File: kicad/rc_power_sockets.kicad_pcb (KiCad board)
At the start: 2 copper layers, 17 parts, among them IC1 ATTINY85-P, J1 Motion Sensor, J2 Radio 433MHZ, P1 ICSP, Q1 N-Channel Mosfet, Q2 P-Channel Mosfet, SW1 SPST, U1 LDO 3v3 Voltage Regulator

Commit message: GND pin on header
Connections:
- J2 pad 1: Net-(C1-Pad1) -> GND
- J2 pad 3: GND -> Net-(C1-Pad1)
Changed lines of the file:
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@@
     (pad_to_mask_clearance 0.2)
     (aux_axis_origin 0 0)
-    (visible_elements FFFFF77F)
+    (visible_elements 7FFFFFFF)
     (pcbplotparams
       (layerselection 0x00030_80000001)
@@
     (fp_line (start -1.55 -1.55) (end 1.55 -1.55) (layer F.SilkS) (width 0.15))
     (pad 1 thru_hole rect (at 0 0) (size 2.032 1.7272) (drill 1.016) (layers *.Cu *.Mask F.SilkS)
-      (net 1 "Net-(C1-Pad1)"))
+      (net 2 GND))
     (pad 2 thru_hole oval (at 0 2.54) (size 2.032 1.7272) (drill 1.016) (layers *.Cu *.Mask F.SilkS)
       (net 9 /RADIO_DATA))
     (pad 3 thru_hole oval (at 0 5.08) (size 2.032 1.7272) (drill 1.016) (layers *.Cu *.Mask F.SilkS)
-      (net 2 GND))
+      (net 1 "Net-(C1-Pad1)"))
     (model Pin_Headers.3dshapes/Pin_Header_Straight_1x03.wrl
       (at (xyz 0 -0.1 0))

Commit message: SMD ATTiny
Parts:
- added C3: 0.1uf, Capacitors_SMD:C_1206_HandSoldering, F.Cu at (146.1, 82.5)
- IC1: value ATTINY85-P -> ATTINY85-S; footprint Housings_DIP:DIP-8_W7.62mm_LongPads -> SMD_Packages:SOIC-8-N
- J1, J2: footprint Pin_Headers:Pin_Header_Straight_1x03 -> Socket_Strips:Socket_Strip_Straight_1x03
- SW1: value SPST -> Power Switch; footprint Wire_Pads:SolderWirePad_2x_2-5mmDrill -> Buttons_Switches_ThroughHole:SW_Micro_SPST_Angled
- moved SW1 56.6 mm to (118.1, 106.7), turned to 0 degrees
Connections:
- SW1 pad 1: Net-(J1-Pad3) -> +BATT

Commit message: Use existing parts
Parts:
- added R5: 100K, Resistors_SMD:R_0805_HandSoldering, F.Cu at (86.4, 96.5)
- added RV1: POT, Potentiometers:Potentiometer_WirePads_largePads, F.Cu at (92.7, 100.3)
- C1, C2, C3: footprint Capacitors_SMD:C_1206_HandSoldering -> Capacitors_SMD:C_0805_HandSoldering
- D1, D2: footprint SMD_Packages:SMD-1206_Pol -> Diodes_SMD:SOD-123
- Q1: value N-Channel Mosfet -> Q_NMOS_GSD
- Q2: value P-Channel Mosfet -> Q_PMOS_GSD
- R1, R2, R3, R4: footprint Resistors_SMD:R_1206_HandSoldering -> Resistors_SMD:R_0805_HandSoldering
- SW1: footprint Buttons_Switches_ThroughHole:SW_Micro_SPST_Angled -> Buttons_Switches_ThroughHole:SW_Micro_SPST
- U1: value LDO 3v3 Voltage Regulator -> MCP1700T-3302E/TT
- moved D1 4.02 mm to (156.2, 91.4)
- moved D2 1.80 mm to (156.2, 99.1)
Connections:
- net +BATT renamed VCC
- IC1 pad 2: Net-(IC1-Pad2) -> /ADC3
- Q1 pad 2: Net-(Q1-Pad2) -> GND
- Q1 pad 3: GND -> Net-(Q1-Pad3)
- Q2 pad 1: Net-(Q1-Pad2) -> Net-(Q1-Pad3)
- R2 pad 2: Net-(Q1-Pad2) -> Net-(Q1-Pad3)

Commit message: 50mm x 50mm
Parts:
- moved R5 142.0 mm to (226.0, 71.0)
- moved RV1 134.7 mm to (225.0, 75.0)
- moved SW1 99.2 mm to (217.0, 99.0)
- moved J2 95.8 mm to (215.0, 71.0)
- moved Q1 71.8 mm to (206.0, 79.0)
- moved R3 71.0 mm to (200.0, 80.0), turned to 180 degrees
- moved Q2 70.5 mm to (211.0, 79.0)
- moved R1 66.8 mm to (200.0, 75.0), turned to 180 degrees
- moved IC1 66.5 mm to (206.0, 88.0)
- moved R4 65.7 mm to (199.0, 91.0), turned to 180 degrees
- moved JP1 65.5 mm to (199.0, 96.0)
- moved D2 65.3 mm to (218.0, 78.0)
- moved P1 63.1 mm to (208.0, 96.0)
- moved D1 62.7 mm to (218.0, 81.0)
- moved R2 62.0 mm to (200.0, 71.0), turned to 0 degrees
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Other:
- board outline added: 50 x 50 mm

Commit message: Layout
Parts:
- C3, R4: moved to B.Cu
- IC1: value ATTINY85-S -> ATTINY85
- JP1: value Jumper_NO_Small -> Jumper
- RV1: footprint Potentiometers:Potentiometer_WirePads_largePads -> Potentiometers:Potentiometer_WirePads_Small
- SW1: value Power Switch -> SPST; footprint Buttons_Switches_ThroughHole:SW_Micro_SPST -> Pin_Headers:Pin_Header_Straight_1x02
- U1: value MCP1700T-3302E/TT -> 3v3REG
- moved R5 22.4 mm to (218.2, 92.0)
- moved RV1 20.4 mm to (221.0, 95.0), turned to 270 degrees
- moved SW1 19.1 mm to (199.0, 92.5)
- moved R2 18.0 mm to (200.0, 89.0)
- moved R4 11.2 mm to (209.2, 86.5), turned to 0 degrees
- moved D1 10.6 mm to (207.8, 78.2), turned to 270 degrees
- moved C3 10.3 mm to (209.2, 84.0), turned to 0 degrees
- moved Q2 9.28 mm to (202.8, 83.2)
- moved Q1 8.19 mm to (199.0, 83.2), turned to 180 degrees
- moved D2 7.50 mm to (210.5, 78.2), turned to 270 degrees
- moved R1 6.17 mm to (205.2, 78.2), turned to 90 degrees
- moved J1 5.48 mm to (209.8, 67.0)
- moved J2 5.48 mm to (218.8, 67.0)
- moved C2 5.26 mm to (220.2, 85.2), turned to 90 degrees
- moved U1 5.20 mm to (217.2, 85.0)
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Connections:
- SW1 pad 1: VCC -> Net-(J1-Pad3)
- SW1 pad 2: Net-(J1-Pad3) -> VCC
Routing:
- net Net-(C2-Pad1): track 0.00 -> 4.52 mm, vias 0 -> 1
- net /RESET: track 0.00 -> 4.42 mm, vias 0 -> 1
- net Net-(J1-Pad3): track 0.00 -> 3.64 mm

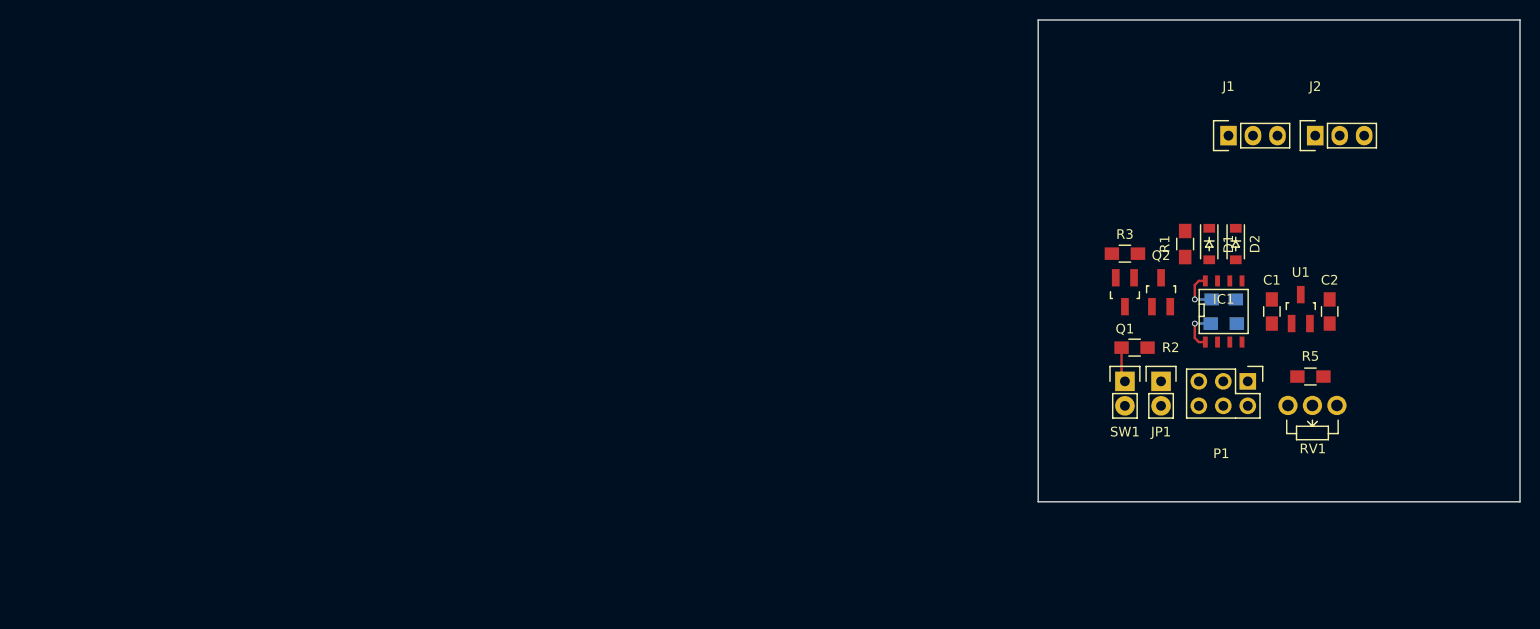
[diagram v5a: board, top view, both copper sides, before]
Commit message: Layout change
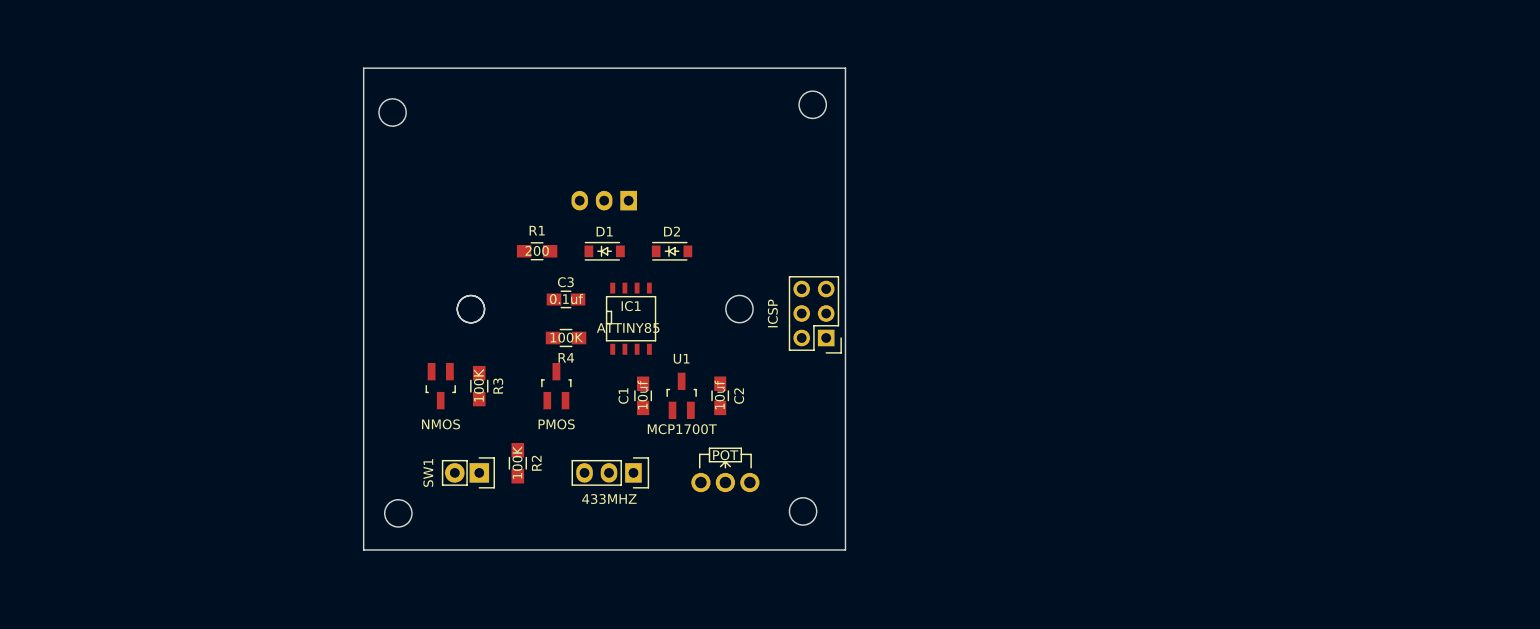
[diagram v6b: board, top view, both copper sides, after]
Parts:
- removed JP1: Jumper, Pin_Headers:Pin_Header_Straight_1x02
- removed R5: 100K, Resistors_SMD:R_0805_HandSoldering
- C3, R4: moved to F.Cu
- J1: value Motion Sensor -> Motion; moved to B.Cu
- J2: value Radio 433MHZ -> 433MHZ
- Q1: value Q_NMOS_GSD -> NMOS
- Q2: value Q_PMOS_GSD -> PMOS
- U1: value 3v3REG -> MCP1700T
- moved J2 78.9 mm to (148.0, 102.0), turned to 180 degrees
- moved Q1 71.7 mm to (128.0, 93.0)
- moved R3 68.4 mm to (132.0, 93.0), turned to 270 degrees
- moved R4 68.3 mm to (141.0, 88.0), turned to 180 degrees
- moved C3 68.2 mm to (141.0, 84.0), turned to 180 degrees
- moved SW1 67.7 mm to (132.0, 102.0), turned to 270 degrees
- moved R1 67.3 mm to (138.0, 79.0), turned to 0 degrees
- moved RV1 66.5 mm to (155.0, 103.0), turned to 90 degrees
- moved C1 65.8 mm to (149.0, 94.0)
- moved R2 65.1 mm to (136.0, 101.0), turned to 90 degrees
- moved U1 64.9 mm to (153.0, 94.0)
- moved C2 63.9 mm to (157.0, 94.0)
- moved Q2 63.5 mm to (140.0, 93.0)
- moved D1 62.8 mm to (145.0, 79.0), turned to 0 degrees
- moved J1 62.6 mm to (147.5, 73.8), turned to 180 degrees
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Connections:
- P1 pad 6: Net-(JP1-Pad2) -> Net-(J1-Pad3)
- RV1 pad 1: Net-(R5-Pad1) -> GND
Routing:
- net Net-(C2-Pad1): track 4.52 -> 0.00 mm, vias 1 -> 0
- net /RESET: track 4.42 -> 0.00 mm, vias 1 -> 0
- net Net-(J1-Pad3): track 3.64 -> 0.00 mm
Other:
- outline, holes or cut-outs redrawn

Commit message: Traces
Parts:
- added J3: 433MHZ, Socket_Strips:Socket_Strip_Straight_1x03, F.Cu at (167.0, 83.0)
- added P2: CONN_GND, Pin_Headers:Pin_Header_Straight_1x01, F.Cu at (155.0, 106.8)
- J1: value Motion -> PIR
- moved RV1 42.3 mm to (124.2, 74.0), turned to 180 degrees
- moved P1 34.7 mm to (142.0, 65.0), turned to 90 degrees
- moved Q1 30.5 mm to (158.5, 93.5)
- moved R3 30.5 mm to (162.5, 93.2)
- moved J2 28.7 mm to (123.0, 88.0), turned to 90 degrees
- moved R4 25.8 mm to (152.8, 65.0), turned to 0 degrees
- moved C2 25.3 mm to (149.8, 69.8), turned to 0 degrees
- moved R2 23.8 mm to (159.5, 97.5), turned to 0 degrees
- moved J1 22.8 mm to (147.3, 96.5)
- moved U1 20.1 mm to (149.5, 74.2), turned to 180 degrees
- moved C1 19.1 mm to (155.2, 76.0), turned to 0 degrees
- moved R1 19.0 mm to (154.0, 89.2), turned to 180 degrees
- moved IC1 15.6 mm to (137.5, 74.2), turned to 270 degrees
- moved C3 14.3 mm to (142.0, 69.8), turned to 0 degrees
- moved Q2 14.0 mm to (154.0, 93.5), turned to 180 degrees
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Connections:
- net Net-(D1-Pad1) renamed /NBASE_ON
- net Net-(Q1-Pad1) renamed /NBASE
- net Net-(Q1-Pad3) renamed /PBASE
- C1 pad 1: Net-(C1-Pad1) -> /SWITCH_POWER
- C2 pad 1: Net-(C2-Pad1) -> /3.3v
- C3 pad 1: Net-(C2-Pad1) -> /3.3v
- IC1 pad 8: Net-(C2-Pad1) -> /3.3v
- J1 pad 3: Net-(J1-Pad3) -> /POWER
- J2 pad 2: /RADIO_DATA -> /SWITCH_POWER
- J2 pad 3: Net-(C1-Pad1) -> /RADIO_DATA
- P1 pad 2: /SCK -> /POWER
- P1 pad 3: /RESET -> /SCK
- P1 pad 4: GND -> /MOSI
- P1 pad 5: /MOSI -> /RESET
- P1 pad 6: Net-(J1-Pad3) -> GND
- Q2 pad 2: Net-(C1-Pad1) -> /SWITCH_POWER
- Q2 pad 3: Net-(J1-Pad3) -> /POWER
- R2 pad 1: Net-(J1-Pad3) -> /POWER
- R4 pad 2: Net-(C2-Pad1) -> /3.3v
- RV1 pad 3: Net-(C2-Pad1) -> /RESET
- SW1 pad 1: Net-(J1-Pad3) -> /POWER
- U1 pad 2: Net-(C2-Pad1) -> /3.3v
- U1 pad 3: Net-(C1-Pad1) -> /SWITCH_POWER
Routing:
- net GND: track 0.00 -> 133.2 mm
- net /SWITCH_POWER: track 0.00 -> 123.9 mm
- net /RADIO_DATA: track 0.00 -> 113.0 mm
- net /SCK: track 0.00 -> 45.4 mm
- net /RESET: track 0.00 -> 45.1 mm
- net /MISO: track 0.00 -> 32.4 mm
- net /POWER: track 0.00 -> 32.1 mm
- net /MOSI: track 0.00 -> 23.6 mm
- net /3.3v: track 0.00 -> 23.0 mm
- net /ADC3: track 0.00 -> 11.0 mm
- net /PBASE: track 0.00 -> 9.41 mm
- net /NBASE: track 0.00 -> 9.38 mm
- net /NBASE_ON: track 0.00 -> 7.79 mm

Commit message: grounds
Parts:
- moved Q2 1.00 mm to (153.0, 93.5)
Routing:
- net GND: track 133.2 -> 198.3 mm, vias 0 -> 5
- net /POWER: track 32.1 -> 29.8 mm
- net /SWITCH_POWER: track 123.9 -> 122.9 mm
- net /PBASE: track 9.41 -> 10.2 mm
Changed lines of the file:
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@@
   (general
     (links 42)
-    (no_connects 8)
-    (area 119.924999 59.924999 170.075001 110.075001)
+    (no_connects 1)
+    (area 118.625 59.899999 170.100001 110.100001)
     (thickness 1.6)
     (drawings 13)
-    (tracks 137)
+    (tracks 171)
     (zones 0)
     (modules 20)
@@
   )
   (module TO_SOT_Packages_SMD:SOT-23_Handsoldering (layer F.Cu)
-    (at 154 93.5 180)
+    (at 153 93.5 180)
     (descr "SOT-23, Handsoldering")
     (tags SOT-23)
@@
       (effects (font (size 1 1) (thickness 0.15)))
     )
-    (fp_text value ICSP (at -3 3 180) (layer F.SilkS)
+    (fp_text value ICSP (at 0.75 -3 180) (layer F.SilkS)
       (effects (font (size 1 1) (thickness 0.15)))
     )
@@
   (gr_line (start 170 60) (end 170 110) (angle 90) (layer Edge.Cuts) (width 0.15))
   (gr_line (start 120 60) (end 170 60) (angle 90) (layer Edge.Cuts) (width 0.15))
-  (segment (start 147.08 62.46) (end 156.96 62.46) (width 0.25) (layer B.Cu) (net 1) (status 400000))
-  (segment (start 167 79) (end 167 83) (width 0.25) (layer B.Cu) (net 1) (status 800000))
+  (segment (start 156.5 76) (end 156.5 75.25) (width 0.25) (layer F.Cu) (net 1) (status 400000))
+  (segment (start 156.5 75.25) (end 154 72.75) (width 0.25) (layer F.Cu) (net 1))
+  (segment (start 150.45 72.74886) (end 153.99886 72.74886) (width 0.25) (layer F.Cu) (net 1) (status 400000))
+  (segment (start 154.25 72.5) (end 162 72.5) (width 0.25) (layer B.Cu) (net 1))
+  (segment (start 154 72.75) (end 154.25 72.5) (width 0.25) (layer B.Cu) (net 1))
+  (via (at 154 72.75) (size 0.6) (drill 0.4) (layers F.Cu B.Cu) (net 1))
+  (segment (start 153.99886 72.74886) (end 154 72.75) (width 0.25) (layer F.Cu) (net 1))
+  (segment (start 151 69.75) (end 151 72.19886) (width 0.25) (layer F.Cu) (net 1) (status 400000))
+  (segment (start 151 72.19886) (end 150.45 72.74886) (width 0.25) (layer F.Cu) (net 1) (status 800000))
+  (segment (start 143.25 69.75) (end 144.25 69.75) (width 0.25) (layer F.Cu) (net 1) (status 400000))
+  (segment (start 146.25 67.75) (end 162 67.75) (width 0.25) (layer B.Cu) (net 1))
+  (segment (start 146 68) (end 146.25 67.75) (width 0.25) (layer B.Cu) (net 1))
+  (via (at 146 68) (size 0.6) (drill 0.4) (layers F.Cu B.Cu) (net 1))
+  (segment (start 144.25 69.75) (end 146 68) (width 0.25) (layer F.Cu) (net 1))
+  (segment (start 134.325 76.155) (end 131.845 76.155) (width 0.25) (layer F.Cu) (net 1) (status 400000))
+  (segment (start 127 79) (end 127 79.5) (width 0.25) (layer B.Cu) (net 1))
+  (segment (start 129.75 76.25) (end 127 79) (width 0.25) (layer B.Cu) (net 1))
+  (segment (start 131.75 76.25) (end 129.75 76.25) (width 0.25) (layer B.Cu) (net 1))
+  (via (at 131.75 76.25) (size 0.6) (drill 0.4) (layers F.Cu B.Cu) (net 1))
+  (segment (start 131.845 76.155) (end 131.75 76.25) (width 0.25) (layer F.Cu) (net 1))
+  (segment (start 162.5 94.6) (end 162.5 97.5) (width 0.25) (layer F.Cu) (net 1) (status 400000))
+  (segment (start 161.25 102) (end 155 102) (width 0.25) (layer B.Cu) (net 1))
+  (segment (start 163.25 100) (end 161.25 102) (width 0.25) (layer B.Cu) (net 1))
+  (segment (start 163.25 98.25) (end 163.25 100) (width 0.25) (layer B.Cu) (net 1))
+  (via (at 163.25 98.25) (size 0.6) (drill 0.4) (layers F.Cu B.Cu) (net 1))
+  (segment (start 162.5 97.5) (end 163.25 98.25) (width 0.25) (layer F.Cu) (net 1))
+  (segment (start 157.55 91.99886) (end 156.00114 91.99886) (width 0.25) (layer F.Cu) (net 1) (status 400000))
+  (segment (start 156 92) (end 155 92) (width 0.25) (layer B.Cu) (net 1))
+  (via (at 156 92) (size 0.6) (drill 0.4) (layers F.Cu B.Cu) (net 1))
+  (segment (start 156.00114 91.99886) (end 156 92) (width 0.25) (layer F.Cu) (net 1))
+  (segment (start 147.08 62.46) (end 156.96 62.46) (width 0.25) (layer B.Cu) (net 1))
+  (segment (start 167 79) (end 167 83) (width 0.25) (layer B.Cu) (net 1))
+  (segment (start 162 72.5) (end 162 74) (width 0.25) (layer B.Cu) (net 1))
   (segment (start 162 74) (end 167 79) (width 0.25) (layer B.Cu) (net 1))
-  (segment (start 162 67.5) (end 162 74) (width 0.25) (layer B.Cu) (net 1))
+  (segment (start 162 67.5) (end 162 67.75) (width 0.25) (layer B.Cu) (net 1))
+  (segment (start 162 67.75) (end 162 72.5) (width 0.25) (layer B.Cu) (net 1))
   (segment (start 156.96 62.46) (end 162 67.5) (width 0.25) (layer B.Cu) (net 1))
-  (segment (start 124.25 74) (end 124.25 76.75) (width 0.25) (layer B.Cu) (net 1) (status 400000))
+  (segment (start 124.25 74) (end 124.25 76.75) (width 0.25) (layer B.Cu) (net 1))
   (segment (start 127 79.5) (end 127 88) (width 0.25) (layer B.Cu) (net 1))
   (segment (start 124.25 76.75) (end 127 79.5) (width 0.25) (layer B.Cu) (net 1))
-  (segment (start 123 88) (end 127 88) (width 0.25) (layer B.Cu) (net 1) (status 400000))
+  (segment (start 123 88) (end 127 88) (width 0.25) (layer B.Cu) (net 1))
   (segment (start 127 88) (end 142 88) (width 0.25) (layer B.Cu) (net 1))
-  (segment (start 147.32 93.32) (end 147.32 96.52) (width 0.25) (layer B.Cu) (net 1) (status 800000))
+  (segment (start 147.32 93.32) (end 147.32 96.52) (width 0.25) (layer B.Cu) (net 1))
   (segment (start 142 88) (end 147.32 93.32) (width 0.25) (layer B.Cu) (net 1))
-  (segment (start 155 106.75) (end 155 82) (width 0.25) (layer B.Cu) (net 1) (status 400000))
-  (segment (start 164.5 80.5) (end 167 83) (width 0.25) (layer B.Cu) (net 1) (status 800000))
+  (segment (start 155 106.75) (end 155 102) (width 0.25) (layer B.Cu) (net 1))
+  (segment (start 155 102) (end 155 92) (width 0.25) (layer B.Cu) (net 1))
+  (segment (start 155 92) (end 155 82) (width 0.25) (layer B.Cu) (net 1))
+  (segment (start 164.5 80.5) (end 167 83) (width 0.25) (layer B.Cu) (net 1))
   (segment (start 156.5 80.5) (end 164.5 80.5) (width 0.25) (layer B.Cu) (net 1))
   (segment (start 155 82) (end 156.5 80.5) (width 0.25) (layer B.Cu) (net 1))
-  (segment (start 155 106.75) (end 151.75 106.75) (width 0.25) (layer B.Cu) (net 1) (status 400000))
-  (segment (start 147.32 102.32) (end 147.32 96.52) (width 0.25) (layer B.Cu) (net 1) (status 800000))
+  (segment (start 155 106.75) (end 151.75 106.75) (width 0.25) (layer B.Cu) (net 1))
+  (segment (start 147.32 102.32) (end 147.32 96.52) (width 0.25) (layer B.Cu) (net 1))
   (segment (start 151.75 106.75) (end 147.32 102.32) (width 0.25) (layer B.Cu) (net 1))
   (segment (start 144.78 96.52) (end 144.78 92.72) (width 0.25) (layer F.Cu) (net 2))
@@
   (segment (start 163 84) (end 163 82) (width 0.25) (layer F.Cu) (net 9))
   (segment (start 164.54 85.54) (end 163 84) (width 0.25) (layer F.Cu) (net 9))
-  (segment (start 153.05 91.99886) (end 150.99886 91.99886) (width 0.25) (layer F.Cu) (net 9))
+  (segment (start 152.05 91.99886) (end 150.99886 91.99886) (width 0.25) (layer F.Cu) (net 9) (status 10))
   (segment (start 149 76.75114) (end 149.5 75.75114) (width 0.25) (layer F.Cu) (net 9))
   (segment (start 149 89.5) (end 149 76.75114) (width 0.25) (layer F.Cu) (net 9))
@@
   (segment (start 159.45 90.2) (end 159.45 91.99886) (width 0.25) (layer F.Cu) (net 11))
   (segment (start 158.5 89.25) (end 159.45 90.2) (width 0.25) (layer F.Cu) (net 11))
-  (segment (start 154 95.00114) (end 154 99) (width 0.25) (layer F.Cu) (net 12))
-  (segment (start 151.25 101.75) (end 143.75 101.75) (width 0.25) (layer F.Cu) (net 12))
-  (segment (start 154 99) (end 151.25 101.75) (width 0.25) (layer F.Cu) (net 12))
+  (segment (start 158.15 97.5) (end 153.5 97.5) (width 0.25) (layer F.Cu) (net 12) (status 400000))
+  (segment (start 153.5 97.5) (end 153 98) (width 0.25) (layer F.Cu) (net 12))
+  (segment (start 153 95.00114) (end 153 98) (width 0.25) (layer F.Cu) (net 12) (status 400000))
+  (segment (start 145.5 100) (end 143.75 101.75) (width 0.25) (layer F.Cu) (net 12))
+  (segment (start 151 100) (end 145.5 100) (width 0.25) (layer F.Cu) (net 12))
+  (segment (start 153 98) (end 151 100) (width 0.25) (layer F.Cu) (net 12))
   (segment (start 143.75 106.5) (end 143.75 101.75) (width 0.25) (layer F.Cu) (net 12))
   (segment (start 143.75 101.75) (end 143.75 101.5) (width 0.25) (layer F.Cu) (net 12))
   (segment (start 143.75 101.5) (end 142.24 99.99) (width 0.25) (layer F.Cu) (net 12))
   (segment (start 142.24 99.99) (end 142.24 96.52) (width 0.25) (layer F.Cu) (net 12))
-  (segment (start 154 95.00114) (end 154 96.5) (width 0.25) (layer F.Cu) (net 12))
-  (segment (start 155 97.5) (end 158.15 97.5) (width 0.25) (layer F.Cu) (net 12))
-  (segment (start 154 96.5) (end 155 97.5) (width 0.25) (layer F.Cu) (net 12))
   (segment (start 160.85 96.1) (end 160.85 97.5) (width 0.25) (layer F.Cu) (net 13))
   (segment (start 158.5 95.00114) (end 159.75114 95.00114) (width 0.25) (layer F.Cu) (net 13))
   (segment (start 159.75114 95.00114) (end 160.85 96.1) (width 0.25) (layer F.Cu) (net 13))
-  (segment (start 154.95 91.99886) (end 154.95 92.7) (width 0.25) (layer F.Cu) (net 13))
-  (segment (start 154.95 92.7) (end 157.25114 95.00114) (width 0.25) (layer F.Cu) (net 13))
+  (segment (start 153.95 91.99886) (end 153.95 92.7) (width 0.25) (layer F.Cu) (net 13) (status 30))
+  (segment (start 153.95 92.7) (end 157.25114 95.00114) (width 0.25) (layer F.Cu) (net 13) (status 10))
   (segment (start 157.25114 95.00114) (end 158.5 95.00114) (width 0.25) (layer F.Cu) (net 13))
   (segment (start 150.135 86) (end 150.135 86.735) (width 0.25) (layer F.Cu) (net 14))
